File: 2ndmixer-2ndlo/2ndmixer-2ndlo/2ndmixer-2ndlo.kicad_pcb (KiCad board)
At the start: 2 copper layers, 73.7 x 48.8 mm, 47 parts, among them J201 Coax Solder Point, J202 Conn_01x02, J203 Coax Solder Point, Q201 2N5179, Q202 2N5109, T201 Bifilar_Transformer, U201 MAV-11BSM+, U202 TUF-1H+, Y201 100MHz

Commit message: various updates
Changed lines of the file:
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@@
     (pad "2" thru_hole circle locked (at 5.08 0 270) (size 1.7018 1.7018) (drill 1.1938) (layers *.Cu *.Mask)
       (net 2 "GND") (pintype "passive"))
+    (model "${KIPRJMOD}/2ndmixer-2ndlo-models/2ndmixer-2ndlo-3D/Trimmer Cap - Brown.stp"
+      (offset (xyz 2.8 0 0))
+      (scale (xyz 1 1 1))
+      (rotate (xyz 0 0 90))
+    )
+    (model "${KIPRJMOD}/2ndmixer-2ndlo-models/2ndmixer-2ndlo-3D/Trimmer Cap - Brown.wrl"
+      (offset (xyz 0 0 0))
+      (scale (xyz 1 1 1))
+      (rotate (xyz 0 0 0))
+    )
   )
   (footprint "Resistor_THT:R_Axial_DIN0207_L6.3mm_D2.5mm_P7.62mm_Horizontal" (layer "F.Cu")
@@
     (pad "2" thru_hole circle locked (at 1.75 0 90) (size 1.8 1.8) (drill 1.2) (layers *.Cu *.Mask)
       (net 2 "GND") (pinfunction "Pin_2") (pintype "passive"))
+    (model "${KIPRJMOD}/2ndmixer-2ndlo-models/2ndmixer-2ndlo-3D/691103110002_1.step"
+      (offset (xyz 0 0 0))
+      (scale (xyz 1 1 1))
+      (rotate (xyz 0 0 0))
+    )
+    (model "${KIPRJMOD}/2ndmixer-2ndlo-models/2ndmixer-2ndlo-3D/691103110002_1.wrl"
+      (offset (xyz 0 0 0))
+      (scale (xyz 1 1 1))
+      (rotate (xyz 0 0 0))
+    )
   )
   (footprint "MountingHole:MountingHole_3.2mm_M3" (layer "F.Cu")
@@
     (pad "4" smd rect locked (at 0 -3.175) (size 0.762 1.4732) (layers "F.Cu" "F.Paste" "F.Mask")
       (net 2 "GND") (pinfunction "GND") (pintype "power_in"))
+    (model "${KIPRJMOD}/2ndmixer-2ndlo-models/2ndmixer-2ndlo-3D/RRR137_MNC.step"
+      (offset (xyz 0 0 0))
+      (scale (xyz 1 1 1))
+      (rotate (xyz 0 0 0))
+    )
   )
   (footprint "Resistor_THT:R_Axial_DIN0207_L6.3mm_D2.5mm_P7.62mm_Horizontal" (layer "F.Cu")
@@
     (pad "4" thru_hole circle locked (at 0 -1.27 90) (size 1.11 1.11) (drill 0.71) (layers *.Cu *.Mask)
       (net 2 "GND") (pinfunction "SHIELD") (pintype "passive"))
+    (model "${KIPRJMOD}/2ndmixer-2ndlo-models/2ndmixer-2ndlo-3D/to-72.step"
+      (offset (xyz 0 0 0))
+      (scale (xyz 1 1 1))
+      (rotate (xyz 0 0 0))
+    )
+    (model "${KIPRJMOD}/2ndmixer-2ndlo-models/2ndmixer-2ndlo-3D/to-72.wrl"
+      (offset (xyz 0 0 0))
+      (scale (xyz 1 1 1))
+      (rotate (xyz 0 0 0))
+    )
   )
   (footprint "Resistor_THT:R_Axial_DIN0207_L6.3mm_D2.5mm_P7.62mm_Horizontal" (layer "F.Cu")
@@
     (pad "2" thru_hole circle (at 0 5.6) (size 2.6 2.6) (drill 1.3) (layers *.Cu *.Mask)
       (net 12 "Net-(C212-Pad1)") (pintype "passive"))
-    (model "${KICAD6_3DMODEL_DIR}/Inductor_THT.3dshapes/L_Toroid_Vertical_L13.0mm_W6.5mm_P5.60mm.wrl"
+    (model "${KIPRJMOD}/2ndmixer-2ndlo-models/2ndmixer-2ndlo-3D/T37-6 IND004.step"
+      (offset (xyz 0 0 0))
+      (scale (xyz 1 1 1))
+      (rotate (xyz 0 0 0))
+    )
+    (model "${KIPRJMOD}/2ndmixer-2ndlo-models/2ndmixer-2ndlo-3D/T37-6 IND004.wrl"
       (offset (xyz 0 0 0))
       (scale (xyz 1 1 1))
@@
     (pad "2" thru_hole circle (at 0 5.6) (size 2.6 2.6) (drill 1.3) (layers *.Cu *.Mask)
       (net 2 "GND") (pintype "passive"))
-    (model "${KICAD6_3DMODEL_DIR}/Inductor_THT.3dshapes/L_Toroid_Vertical_L13.0mm_W6.5mm_P5.60mm.wrl"
+    (model "${KIPRJMOD}/2ndmixer-2ndlo-models/2ndmixer-2ndlo-3D/T37-6 IND004.step"
+      (offset (xyz 0 0 0))
+      (scale (xyz 1 1 1))
+      (rotate (xyz 0 0 0))
+    )
+    (model "${KIPRJMOD}/2ndmixer-2ndlo-models/2ndmixer-2ndlo-3D/T37-6 IND004.wrl"
       (offset (xyz 0 0 0))
       (scale (xyz 1 1 1))
@@
     (pad "3" thru_hole circle (at 15 0) (size 3 3) (drill 1.2) (layers *.Cu *.Mask)
       (net 23 "Net-(Q202-PadC)") (pinfunction "3") (pintype "passive"))
-    (model "${KICAD6_3DMODEL_DIR}/Transformer_THT.3dshapes/Autotransformer_Toroid_1Tap_Horizontal_D10.5mm_Amidon-T37.wrl"
-      (offset (xyz 0 0 0))
+    (model "${KIPRJMOD}/2ndmixer-2ndlo-models/2ndmixer-2ndlo-3D/L_Tor_13x8x5_3a_cp.step"
+      (offset (xyz 0 -5 0))
+      (scale (xyz 1 1 1))
+      (rotate (xyz 0 0 0))
+    )
+    (model "${KIPRJMOD}/2ndmixer-2ndlo-models/2ndmixer-2ndlo-3D/L_Tor_13x8x5_3a_cp.wrl"
+      (offset (xyz 0 -5 0))
       (scale (xyz 1 1 1))
       (rotate (xyz 0 0 0))
@@
     (pad "2" thru_hole circle (at 0 5.6) (size 2.6 2.6) (drill 1.3) (layers *.Cu *.Mask)
       (net 5 "Net-(C204-Pad1)") (pintype "passive"))
-    (model "${KICAD6_3DMODEL_DIR}/Inductor_THT.3dshapes/L_Toroid_Vertical_L13.0mm_W6.5mm_P5.60mm.wrl"
+    (model "${KIPRJMOD}/2ndmixer-2ndlo-models/2ndmixer-2ndlo-3D/T37-6 IND004.step"
+      (offset (xyz 0 0 0))
+      (scale (xyz 1 1 1))
+      (rotate (xyz 0 0 0))
+    )
+    (model "${KIPRJMOD}/2ndmixer-2ndlo-models/2ndmixer-2ndlo-3D/T37-6 IND004.wrl"
       (offset (xyz 0 0 0))
       (scale (xyz 1 1 1))
@@
     (effects (font (size 1 1) (thickness 0.2)))
   )
-  (gr_text "In" (at 108.3818 113.3348) (layer "F.SilkS")
+  (gr_text "In" (at 106.2736 115.6462 90) (layer "F.SilkS")
     (effects (font (size 1.5 1.5) (thickness 0.3)))
   )
-  (gr_text "Out" (at 165.1508 123.3932) (layer "F.SilkS")
+  (gr_text "Out" (at 164.465 120.9548 90) (layer "F.SilkS")
     (effects (font (size 1.5 1.5) (thickness 0.3)))
   )

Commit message: updates to 2ndmixer-2ndlo
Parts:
- removed the C214 at (157.6, 109.8)
- added L202: 420n, Inductor_THT:L_Toroid_Vertical_L13.0mm_W6.5mm_P5.60mm, F.Cu at (162.7, 98.6)
- added TP201: TestPoint, TestPoint:TestPoint_Pad_1.0x1.0mm, F.Cu at (111.8, 93.8)
- added TP202: TestPoint, TestPoint:TestPoint_Pad_1.0x1.0mm, F.Cu at (123.7, 81.8)
- added TP203: TestPoint, TestPoint:TestPoint_Pad_1.0x1.0mm, F.Cu at (109.6, 113.8)
- added TP204: TestPoint, TestPoint:TestPoint_Pad_1.0x1.0mm, F.Cu at (129.7, 108.1)
- added TP205: TestPoint, TestPoint:TestPoint_Pad_1.0x1.0mm, F.Cu at (139.5, 108.1)
- added TP206: TestPoint, TestPoint:TestPoint_Pad_1.0x1.0mm, F.Cu at (136.1, 123.4)
- added TP207: TestPoint, TestPoint:TestPoint_Pad_1.0x1.0mm, F.Cu at (149.0, 122.6)
- added TP208: TestPoint, TestPoint:TestPoint_Pad_1.0x1.0mm, F.Cu at (147.1, 112.1)
- added TP209: TestPoint, TestPoint:TestPoint_Pad_1.0x1.0mm, F.Cu at (165.5, 90.0)
- added TP210: TestPoint, TestPoint:TestPoint_Pad_1.0x1.0mm, F.Cu at (166.1, 94.3)
- C204: value 15 -> 33
- C205: value 82 -> 33
- C211: value 120u -> 120p
- L201: value 57n -> 40n
- L203: renamed from L202; value .1u -> 1u
- L204: renamed from L203; value .3u -> 1u
- Q202: value 2N5109 -> 2N5179; footprint 2ndmixer-2ndlo:TO5A -> 2ndmixer-2ndlo:TO127P584H533-4N
- moved C212 9.70 mm to (163.7, 107.6)
- moved C214 9.19 mm to (167.3, 114.4)
- moved R217 8.48 mm to (161.0, 111.0)
- moved C211 7.56 mm to (158.6, 111.1)
- moved R212 7.44 mm to (153.6, 107.6)
- moved R216 5.61 mm to (159.6, 117.6)
- moved R215 5.36 mm to (121.9, 77.7)
- moved R214 4.93 mm to (159.4, 114.5)
- moved C204 2.76 mm to (117.9, 98.8)
- moved L201 2.34 mm to (117.4, 84.4)
- moved J203 2.19 mm to (163.8, 121.5), turned to 180 degrees
- moved R204 2.09 mm to (111.9, 81.1)
- moved U201 1.88 mm to (142.4, 120.0)
- moved R210 1.83 mm to (111.8, 77.7)
- moved U202 1.63 mm to (134.2, 111.3)
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- renumbered C203 to C201, C202 to C203, C215 to C214, R203 to R202, R202 to R203
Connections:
- J203 pad 1: Net-(C214-Pad2) (its old number) -> Net-(J203-Pad1)
- R213 pad 1: Net-(Q202-PadC) -> Net-(Q202-Pad3)
- R216 pad 1: Net-(Q202-PadE) -> Net-(Q202-Pad1)
- R217 pad 1: Net-(Q202-PadE) -> Net-(Q202-Pad1)
- T201 pad 2: Net-(C214-Pad1) -> Net-(J203-Pad1)
- T201 pad 3: Net-(Q202-PadC) -> Net-(Q202-Pad3)
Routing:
- net Net-(L202-Pad2): track 23.8 -> 72.7 mm
- net Net-(C204-Pad2): track 11.7 -> 51.7 mm
- net Net-(Q202-Pad1): track 0.00 -> 36.3 mm
- net Net-(J203-Pad1): track 0.00 -> 35.3 mm
- net Net-(Q202-PadE): track 30.1 -> 0.00 mm
- net Net-(C214-Pad1): track 19.5 -> 0.00 mm
- net Net-(Q202-Pad3): track 0.00 -> 16.9 mm
- net Net-(C209-Pad1): track 14.6 -> 29.6 mm
- net Net-(C214-Pad2) (its old number): track 11.9 -> 0.00 mm
- net Net-(C212-Pad2): track 7.32 -> 18.4 mm
- net Net-(Q202-PadC): track 10.1 -> 0.00 mm
- net Net-(L204-Pad1): track 22.2 -> 30.3 mm
- net Net-(C207-Pad2): track 18.8 -> 26.3 mm
- net /+15: track 24.8 -> 31.5 mm
- net Net-(C212-Pad1): track 10.4 -> 16.4 mm
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
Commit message: 2ndmixer-2ndlo bom and corrections
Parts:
- C201, C203: value 470u -> 470p
- C204, C205: value 33 -> 33p
- C206: value 10u-50u -> 12p-60p
- C207: value 15 -> 15p
- C208: value 82 -> 82p
- U201: value MAV-11BSM+ -> MAV-11
- moved U201 0.14 mm to (142.3, 119.9)

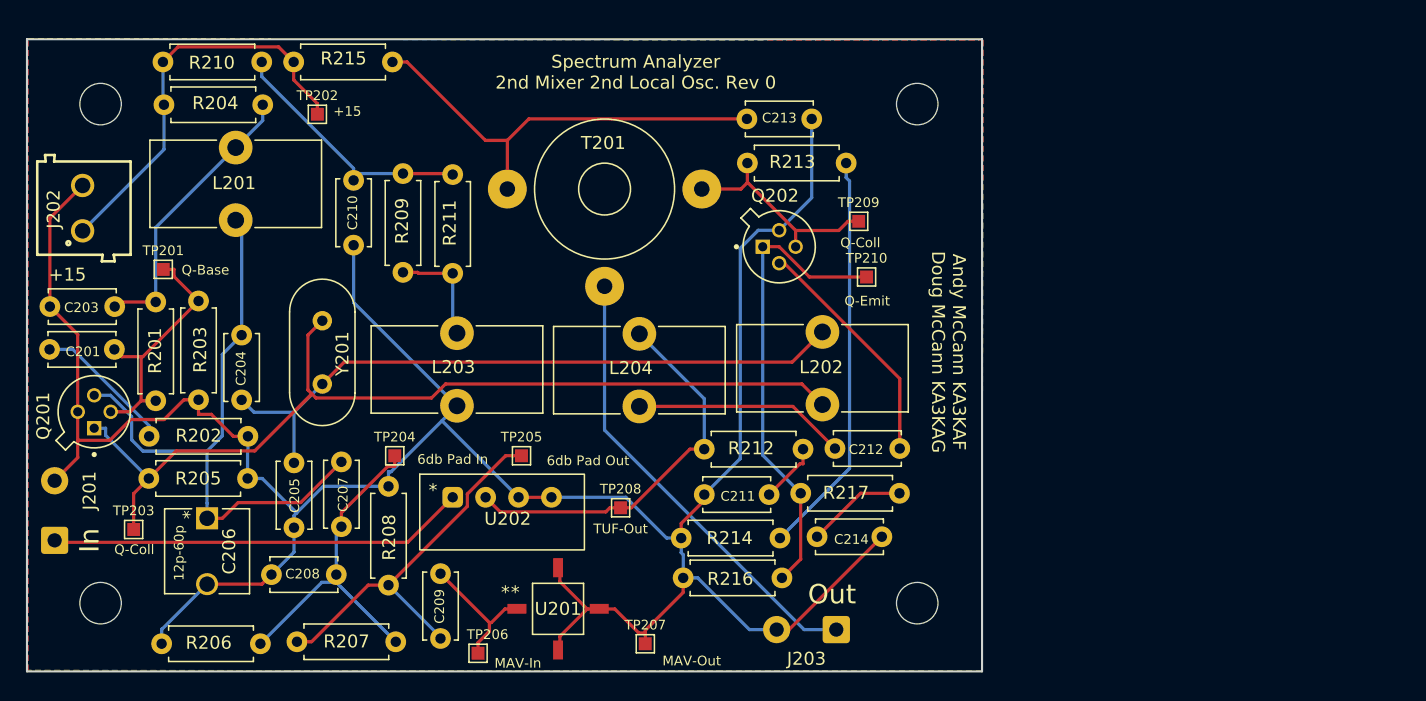
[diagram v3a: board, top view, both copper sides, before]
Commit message: 2ndmixer-2ndlo pcb fix
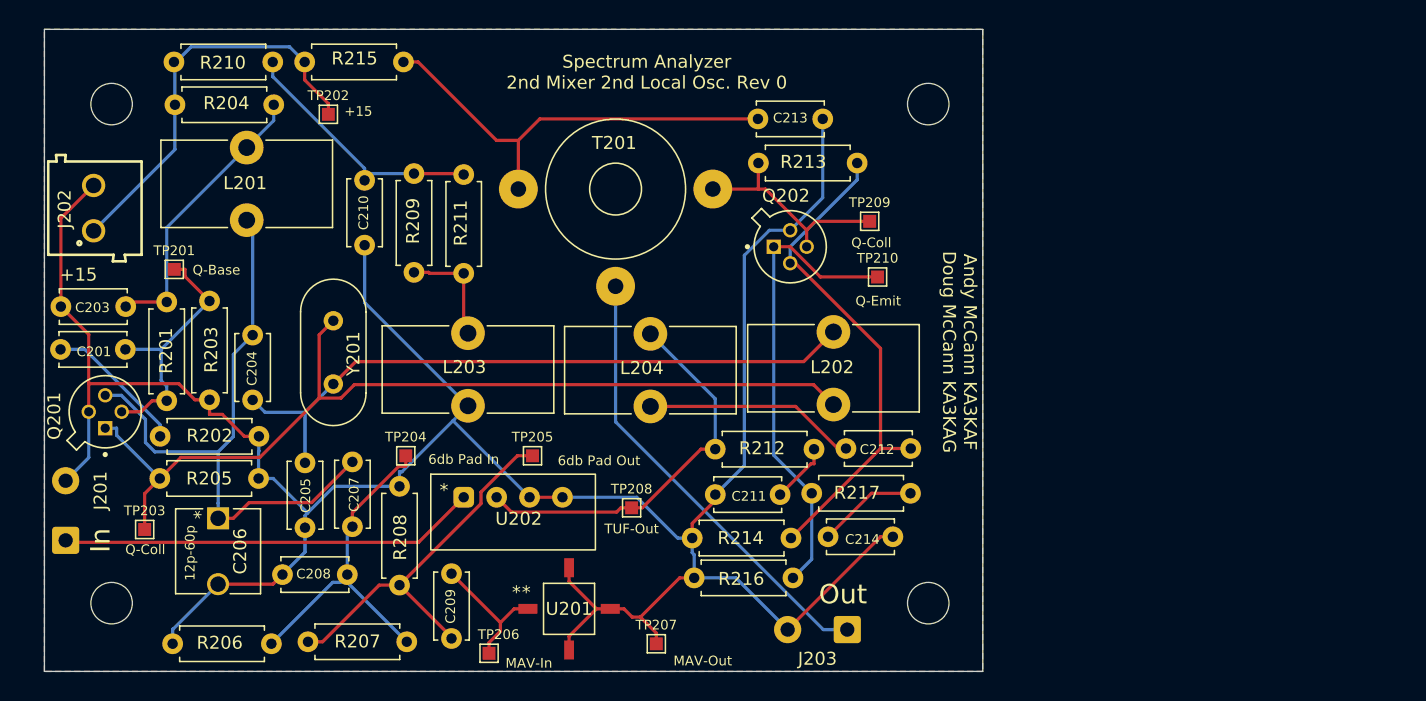
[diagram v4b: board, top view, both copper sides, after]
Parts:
- moved C212 0.85 mm to (164.5, 107.6)
- moved L203 0.85 mm to (135.3, 98.7)
- moved Q202 0.85 mm to (160.2, 92.0)
- moved R207 0.85 mm to (130.6, 122.5)
- moved TP204 0.85 mm to (130.5, 108.1)
- moved TP205 0.85 mm to (140.3, 108.1)
- moved TP206 0.85 mm to (137.0, 123.4)
- moved TP209 0.85 mm to (166.3, 90.0)
- moved TP210 0.85 mm to (166.9, 94.3)
- moved U201 0.85 mm to (143.1, 119.9)
- moved C201 0.85 mm to (108.9, 99.9)
- moved C203 0.85 mm to (108.9, 96.6)
- moved C204 0.85 mm to (118.7, 98.8)
- moved C205 0.85 mm to (122.8, 108.7)
- moved C206 0.85 mm to (116.1, 113.0)
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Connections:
- R213 pad 2: Net-(R213-Pad2) -> Net-(C212-Pad2)
- R214 pad 1: Net-(R213-Pad2) -> Net-(C212-Pad2)
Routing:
- net Net-(R213-Pad2): track 31.3 -> 0.00 mm
- net Net-(C212-Pad2): track 18.4 -> 39.4 mm
- net GND: track 201.3 -> 200.6 mm
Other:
- board size 73.7 x 48.8 mm -> 72.4 x 49.5 mm

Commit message: minor changes to 5 boards
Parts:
- TP201: value TestPoint -> Q-Base
- TP202: value TestPoint -> +15
- TP203, TP209: value TestPoint -> Q-Coll
- TP204: value TestPoint -> 6db Pad In
- TP205: value TestPoint -> 6db Pad Out
- TP206: value TestPoint -> MAV-In
- TP207: value TestPoint -> MAV-Out
- TP208: value TestPoint -> TUF-Out
- TP210: value TestPoint -> Q-Emit
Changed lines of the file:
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@@
       (effects (font (size 0.75 0.75) (thickness 0.15)))
     )
-    (fp_text value "TestPoint" (at 0 1.55) (layer "F.Fab")
+    (fp_text value "Q-Base" (at 0 1.55) (layer "F.Fab")
       (effects (font (size 1 1) (thickness 0.15)))
     )
@@
       (effects (font (size 0.75 0.75) (thickness 0.15)))
     )
-    (fp_text value "TestPoint" (at 0 1.55) (layer "F.Fab")
+    (fp_text value "Q-Coll" (at 0 1.55) (layer "F.Fab")
       (effects (font (size 1 1) (thickness 0.15)))
     )
@@
       (effects (font (size 0.75 0.75) (thickness 0.15)))
     )
-    (fp_text value "TestPoint" (at 0 1.55) (layer "F.Fab")
+    (fp_text value "Q-Coll" (at 0 1.55) (layer "F.Fab")
       (effects (font (size 1 1) (thickness 0.15)))
     )
@@
       (effects (font (size 0.75 0.75) (thickness 0.15)))
     )
-    (fp_text value "TestPoint" (at 0 1.55) (layer "F.Fab")
+    (fp_text value "6db Pad In" (at 0 1.55) (layer "F.Fab")
       (effects (font (size 1 1) (thickness 0.15)))
     )
@@
       (effects (font (size 0.75 0.75) (thickness 0.15)))
     )
-    (fp_text value "TestPoint" (at 0 1.55) (layer "F.Fab")
+    (fp_text value "+15" (at 0 1.55) (layer "F.Fab")
       (effects (font (size 1 1) (thickness 0.15)))
     )
@@
       (effects (font (size 0.75 0.75) (thickness 0.15)))
     )
-    (fp_text value "TestPoint" (at 0 1.55) (layer "F.Fab")
+    (fp_text value "MAV-In" (at 0 1.55) (layer "F.Fab")
       (effects (font (size 1 1) (thickness 0.15)))
     )
@@
       (effects (font (size 0.75 0.75) (thickness 0.15)))
     )
-    (fp_text value "TestPoint" (at 0 1.55) (layer "F.Fab")
+    (fp_text value "6db Pad Out" (at 0 1.55) (layer "F.Fab")
       (effects (font (size 1 1) (thickness 0.15)))
     )
@@
       (effects (font (size 0.75 0.75) (thickness 0.15)))
     )
-    (fp_text value "TestPoint" (at 0 1.55) (layer "F.Fab")
+    (fp_text value "TUF-Out" (at 0 1.55) (layer "F.Fab")
       (effects (font (size 1 1) (thickness 0.15)))
     )
@@
       (effects (font (size 0.75 0.75) (thickness 0.15)))
     )
-    (fp_text value "TestPoint" (at 0 1.55) (layer "F.Fab")
+    (fp_text value "MAV-Out" (at 0 1.55) (layer "F.Fab")
       (effects (font (size 1 1) (thickness 0.15)))
     )
@@
       (effects (font (size 0.75 0.75) (thickness 0.15)))
     )
-    (fp_text value "TestPoint" (at 0 1.55) (layer "F.Fab")
-      (effects (font (size 1 1) (thickness 0.15)))
-    )
+    (fp_text value "Q-Emit" (at 0 1.55) (layer "F.Fab")
+      (effects (font (size 1 1) (thickness 0.15)))
+    )

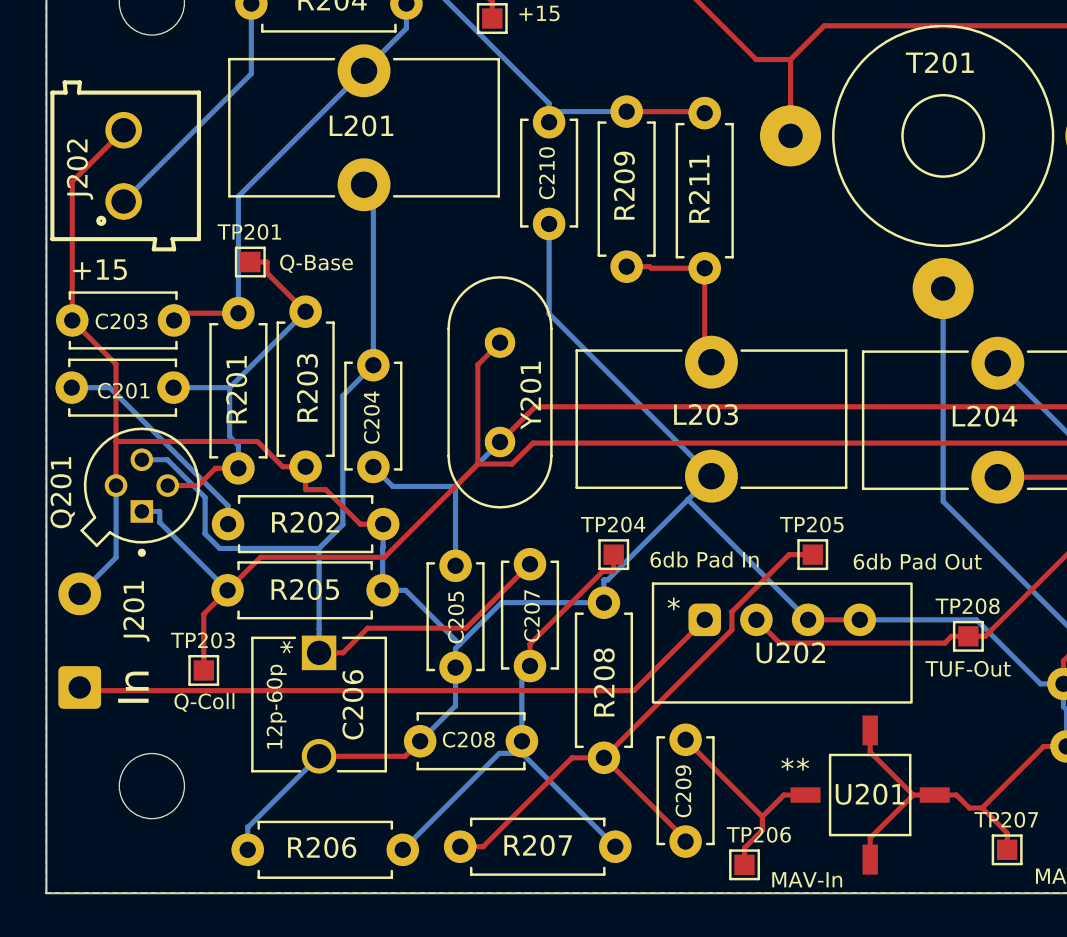
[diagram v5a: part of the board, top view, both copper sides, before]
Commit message: Fixes to 2ndmixer-2ndlo and vco-1stmixer
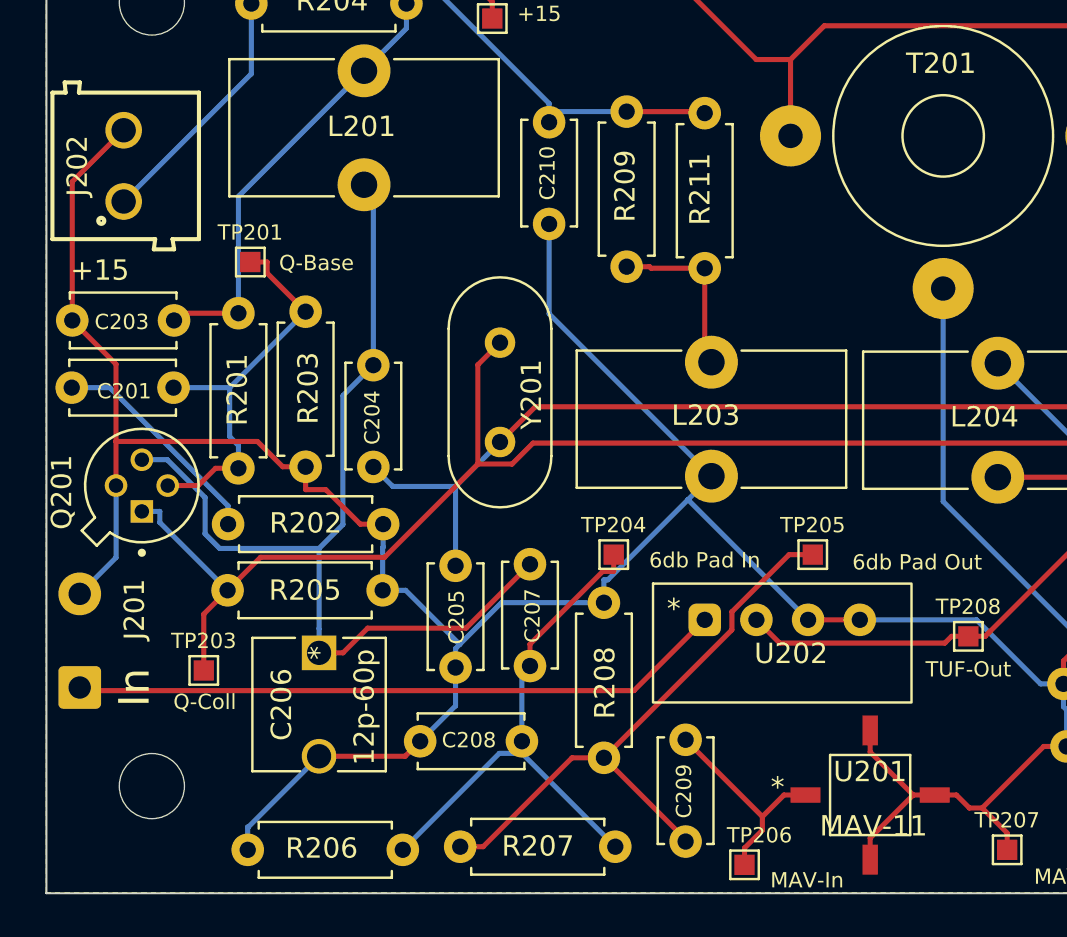
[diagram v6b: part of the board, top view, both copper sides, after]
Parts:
- C206: footprint 2ndmixer-2ndlo:GKG60015 -> spectrum_analyzer:GKG60015
- J202: footprint 2ndmixer-2ndlo:691103110002 -> spectrum_analyzer:691103110002
- Q201, Q202: footprint 2ndmixer-2ndlo:TO127P584H533-4N -> spectrum_analyzer:TO127P584H533-4N
- U201: footprint 2ndmixer-2ndlo:MAV-11BSM&plus_ -> spectrum_analyzer:MAV-11BSM&plus_
